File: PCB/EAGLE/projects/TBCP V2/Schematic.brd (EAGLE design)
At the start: 160 x 71.1 mm, 111 parts, among them J1 FP Header, J100 ADS1115, J2 12 Supply, J3 TB Header, Q1 DMP4025LK3Q-13, U1 ESP32-DEVKITC, U100 TLE9201SG, U2 7805

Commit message: TBCP 2.0 for review
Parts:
- removed SJ1: SOLDERJUMPERTRACE, SparkFun-Retired:SJ_2S-TRACE
- removed SW1: (no value), One_Dimensional_Pong:SWITCH_SPST_SMD_A
- added S5: 500SSP1S1M6QEA, 500SSP1S1M6QEA:500SSP1S1M6QEA
- R1, R11, R2, R3, R5, R8: value (none) -> 150
- R10, R4, R7: value 8000 -> 5k
- R13, R14, R15, R16: value (none) -> 5k
- S1, S2, S3, S4: value (none) -> MOMENTARY-SWITCH-SPST-PTH-6.0MM-KIT; device SparkFun-Retired:TACTILE-SWITCH-SMD -> SparkFun-Switches:TACTILE_SWITCH_PTH_6.0MM_KIT
- moved Q1 6.48 mm to (102.9, 7.62)
- moved Z1 6.48 mm to (111.8, 7.62)
- moved R17 6.48 mm to (115.6, 7.62)
- moved J2 4.58 mm to (62.2, 10.2)
- moved S1 2.84 mm to (19.1, 7.62)
- moved S2 2.84 mm to (29.2, 7.62)
- moved S3 2.84 mm to (39.4, 7.62)
- moved S4 2.84 mm to (49.5, 7.62)
- moved TP104 2.62 mm to (80.0, 43.2)
- moved TP105 1.42 mm to (80.0, 45.7)
- moved TP101 1.27 mm to (80.0, 40.6)
- moved TP102 1.27 mm to (80.0, 35.6)
- moved TP106 0.63 mm to (80.0, 48.3)
- renumbered J100 to U4, U100 to U5
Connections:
- net 0VDC: no longer SJ1.2
- net 3.3VDC: no longer S1.4, S2.4, S3.4, S4.4
- net ADS1115_A4: no longer SJ1.1
- net GPIO34: no longer S3.2
- net GPIO35: no longer S4.2
- net GPIO36: no longer S1.2
- net GPIO39: no longer S2.2
- net N$1: now also S5.2; no longer SW1.3
- net N$36: now also S5.1; no longer SW1.2
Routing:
- net GPIO27: track 80.9 -> 48.5 mm
- net N$1: track 0.00 -> 26.6 mm
- net GPIO35: track 33.6 -> 21.7 mm
- net GPIO36: track 50.3 -> 38.3 mm
- net GPIO34: track 30.7 -> 18.9 mm
- net GPIO39: track 33.9 -> 22.0 mm
- net M0+: track 126.7 -> 136.5 mm
- net M0-: track 133.1 -> 140.3 mm
- net N$36: track 10.5 -> 15.9 mm
- net 12VDC: track 126.2 -> 130.8 mm
- net ADS1115_A4: track 6.48 -> 3.81 mm
- net GPIO26: track 73.2 -> 71.4 mm
- added copper zone on layer 16, net 0VDC
- removed copper zone on layer 16, net 0VDC1
- removed copper zone on layer 1, net N$1
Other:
- board text added: "Project: Throttle Body Control Platform By: Oliver Bell, Piyapat Srisawat Date: 01/08/2024 Version: 2.0"
- board text removed: "Project: Throttle body control Platform By: Oliver Bell, Piyapat Srisawat Date: 01/08/2024 Version: 2.0"

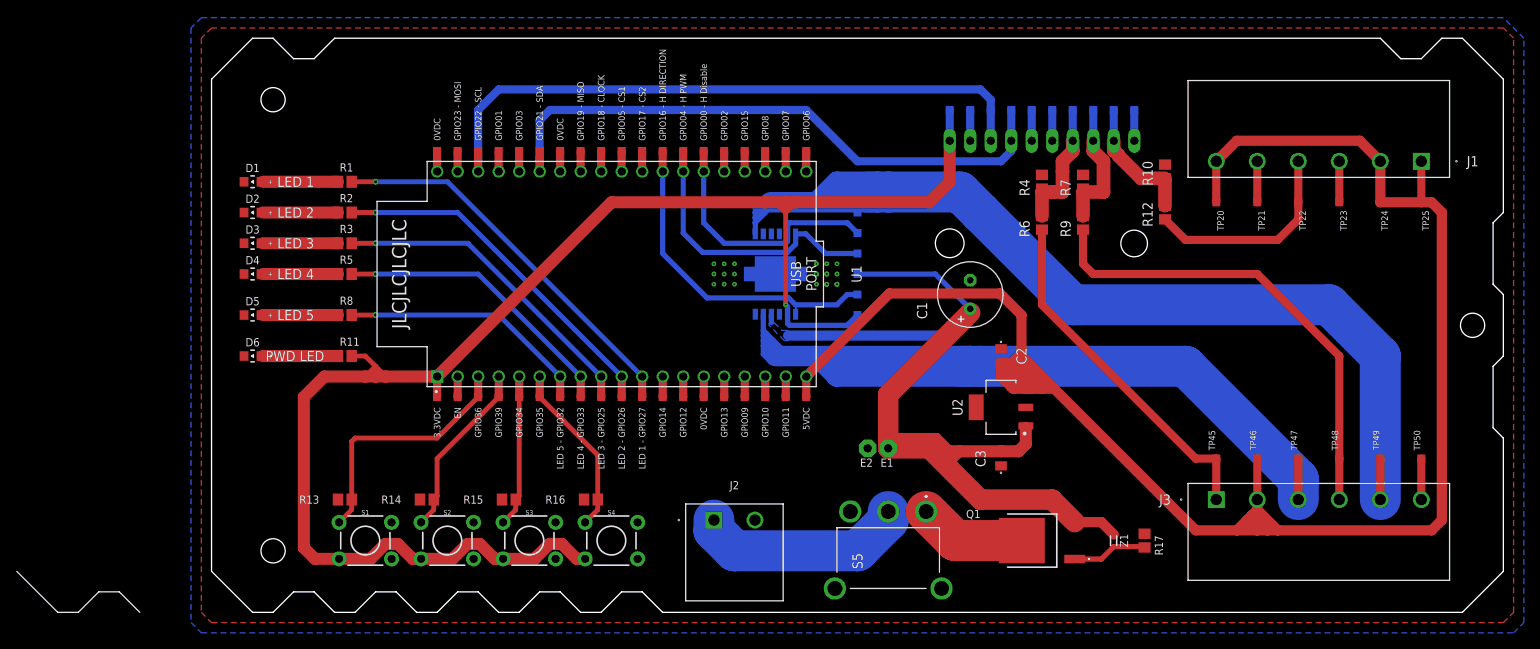
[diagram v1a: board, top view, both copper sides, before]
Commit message: Major rename of folder
matlab doesnt like have spaces in names of files or folders
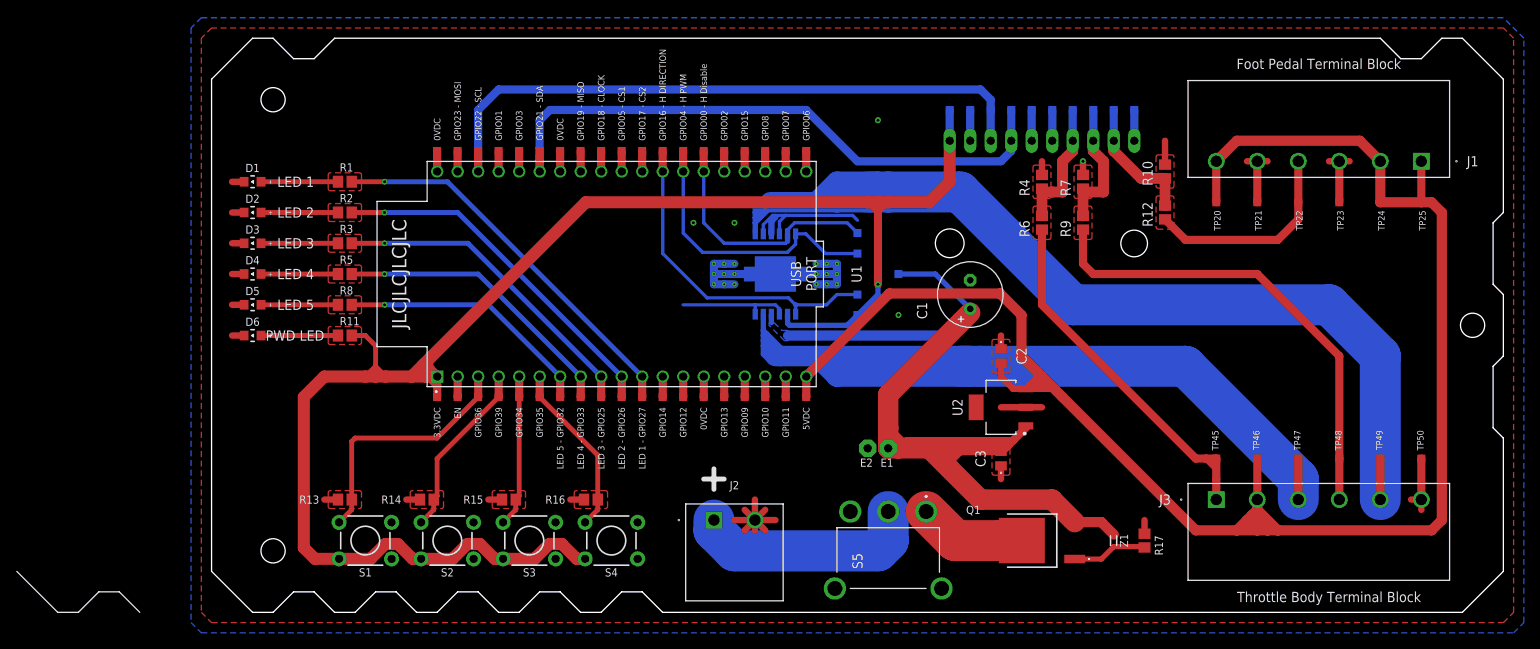
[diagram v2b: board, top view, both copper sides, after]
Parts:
- moved TP101 5.08 mm to (85.1, 40.6)
- moved D6 2.54 mm to (5.08, 33.0)
- moved R11 2.54 mm to (16.5, 33.0)
- moved TP106 1.27 mm to (80.0, 49.5)
- moved D5 1.27 mm to (5.08, 36.8)
- moved R8 1.27 mm to (16.5, 36.8)
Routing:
- net 0VDC: track 26.7 -> 144.6 mm, vias 22 -> 23
- net 12VDC: track 130.8 -> 147.8 mm
- net 3.3VDC: track 198.8 -> 211.4 mm
- net 5VDC: track 231.2 -> 222.1 mm
- net TB_FB_INV: track 43.9 -> 46.9 mm
- net N$1: track 26.6 -> 28.0 mm
- net M0-: track 140.3 -> 139.1 mm
- net N$2: track 9.53 -> 10.2 mm
- net GPIO32: track 31.5 -> 32.1 mm
- added copper zone on layer 1, net 0VDC17
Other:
- board text added: "0VDC 6."
- board text added: "1. 5VDC"
- board text added: "5VDC 2."
- board text added: "Foot Pedal Terminal Block"
- board text added: "M0+ 3."
- board text added: "M0- 5."
- board text added: "TB_FB 4."
- board text added: "TB_FB_INV 1."
- board text added: "Throttle Body Terminal Block"

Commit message: TBCP 2.0 sent to JLCPCB
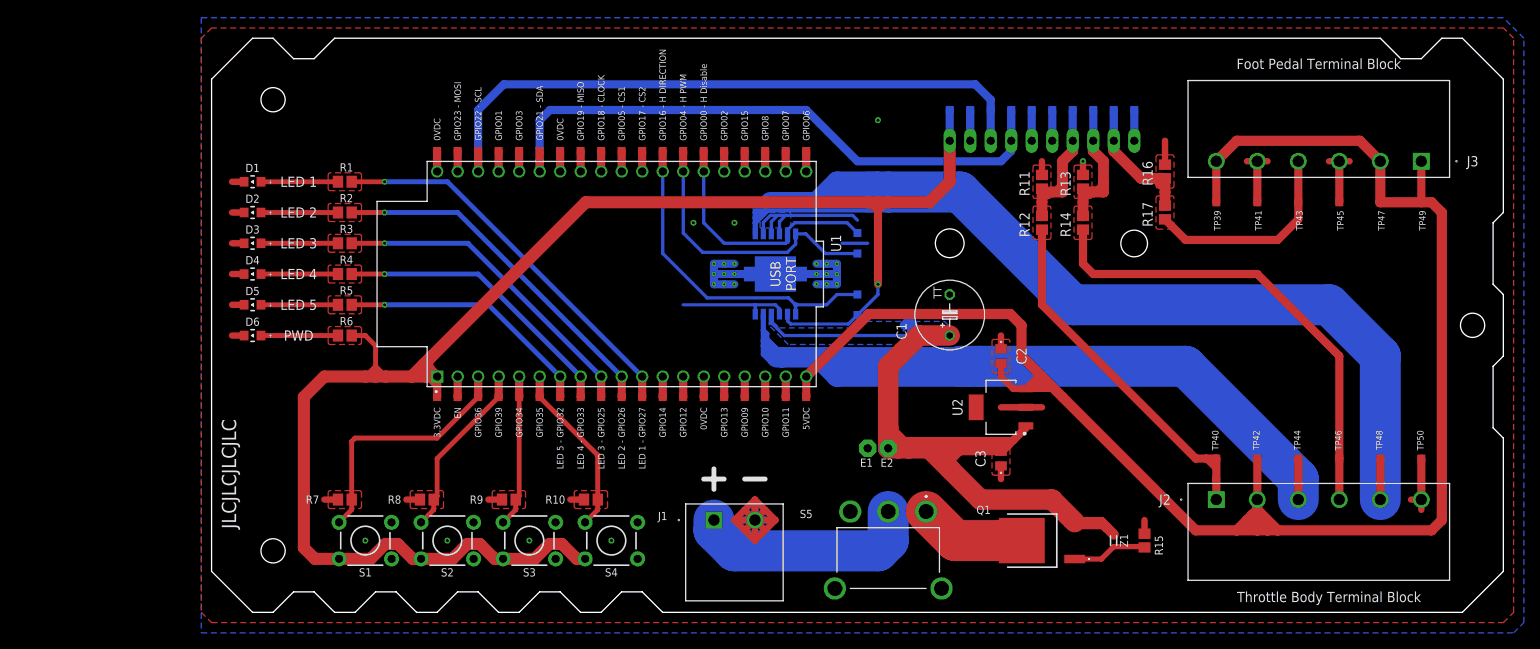
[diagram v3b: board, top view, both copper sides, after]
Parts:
- C1: device BeagleBone_Blue_R3:E3,5-8 -> BeagleBone_Blue_R3:TAP5-80
- J1: value FP Header -> 12 Supply; device Terminal 5.08 Pitch 6S 1757284:1757284 -> Terminal 5.08 Pitch 2S :1757284
- J2: value 12 Supply -> TB Header; device Terminal 5.08 Pitch 2S :1757284 -> Terminal 5.08 Pitch 6S 1757284:1757284
- J3: value TB Header -> FP Header
- R11, R8: value 150 -> 5k
- R14: value 5k -> 100k
- R15: value 5k -> 100K
- R17: value 100K -> 100k
- R4: value 5k -> 150
- R6: value 100k -> 150
- R9: value 100k -> 5k
- TP10: value TESTPOINT_TPS-SMD-10SN -> GPIO34
- TP12: value TESTPOINT_TPS-SMD-10SN -> GPIO35
- TP14: value TESTPOINT_TPS-SMD-10SN -> GPIO32
- TP2: value TESTPOINT_TPS-SMD-10SN -> 3V3
- TP26: value 3V3 -> TESTPOINT_TPS-SMD-10SN
- TP27: value EN -> TESTPOINT_TPS-SMD-10SN
- TP28: value GPIO36 -> TESTPOINT_TPS-SMD-10SN
- TP29: value GPIO39 -> TESTPOINT_TPS-SMD-10SN
- TP30: value GPIO34 -> TESTPOINT_TPS-SMD-10SN
- TP31: value GPIO35 -> TESTPOINT_TPS-SMD-10SN
- TP32: value GPIO32 -> TESTPOINT_TPS-SMD-10SN
- TP4: value TESTPOINT_TPS-SMD-10SN -> EN
- TP6: value TESTPOINT_TPS-SMD-10SN -> GPIO36
- TP8: value TESTPOINT_TPS-SMD-10SN -> GPIO39
- moved R13 99.6 mm to (108.0, 52.1), turned to 270 degrees
- moved R7 99.6 mm to (16.5, 12.7), turned to 180 degrees
- moved J1 98.3 mm to (62.2, 10.2), turned to 0 degrees
- moved TP24 92.1 mm to (55.9, 25.4)
- moved TP25 91.7 mm to (58.4, 55.9), turned to 90 degrees
- moved R11 88.4 mm to (102.9, 52.1), turned to 270 degrees
- moved R14 88.2 mm to (108.0, 47.0), turned to 270 degrees
- moved R6 87.5 mm to (16.5, 33.0), turned to 0 degrees
- moved R4 87.1 mm to (16.5, 40.6), turned to 0 degrees
- moved TP22 84.8 mm to (53.3, 25.4)
- moved TP23 84.1 mm to (55.9, 55.9), turned to 90 degrees
- moved R10 81.9 mm to (47.0, 12.7), turned to 180 degrees
- moved R16 81.9 mm to (118.1, 53.3), turned to 270 degrees
- moved R9 79.0 mm to (36.8, 12.7), turned to 180 degrees
- moved R15 78.9 mm to (115.6, 7.62), turned to 270 degrees
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- renumbered U4 to U100, U5 to U101
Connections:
- net 0VDC: now also E1.PAD, J1.2, J2.6, J3.3, J3.5, R10.2, R11.1, R13.1, R15.1, R16.1, R7.2, R8.2, R9.2, TP108.TP, TP13.TP, TP28.TP, TP41.TP, TP45.TP; no longer E2.PAD, J1.3, J1.5, J2.2, J3.6, R10.1, R13.2, R14.2, R15.2, R16.2, R17.1, R4.1, R7.1, TP115.TP, TP21.TP, TP23.TP, TP39.TP, TP7.TP
- net 12VDC: now also E2.PAD, TP110.TP; no longer E1.PAD, TP101.TP
- net 3.3VDC: now also R6.2, TP109.TP, TP112.TP, TP2.TP; no longer R11.2, TP102.TP, TP116.TP, TP26.TP
- net 5VDC: now also J2.2, J3.1, J3.6, TP38.TP, TP39.TP, TP42.TP, TP47.TP, TP49.TP; no longer J1.1, J1.2, J1.6, TP20.TP, TP24.TP, TP25.TP, TP44.TP, TP46.TP
- net ADDR: now also TP105.TP; no longer TP112.TP
- net ADS1115_A0: now also R11.2, R12.1, TP103.TP; no longer R4.2, R6.1, TP110.TP
- net ADS1115_A1: now also R13.2, R14.1, TP102.TP; no longer R7.2, R9.1, TP109.TP
- net ADS1115_A2: now also R16.2, R17.1, TP101.TP; no longer R10.2, R12.1, TP108.TP
- net ADS1115_A4: now also TP100.TP; no longer TP107.TP
- net EN: now also TP4.TP; no longer TP27.TP
- net FP_FB: now also J3.4, R17.2, TP43.TP; no longer J1.4, R12.2, TP22.TP
- net GPIO01: now also TP7.TP; no longer TP4.TP
- net GPIO02: now also TP29.TP; no longer TP15.TP
- net GPIO03: now also TP9.TP; no longer TP5.TP
- net GPIO06: now also TP37.TP; no longer TP19.TP
- net GPIO07: now also TP35.TP; no longer TP18.TP
- net GPIO08: now also TP33.TP; no longer TP17.TP
- net GPIO09: now also TP32.TP; no longer TP41.TP
- net GPIO10: now also TP34.TP; no longer TP42.TP
- net GPIO11: now also TP36.TP; no longer TP43.TP
- net GPIO12: now also TP26.TP; no longer TP38.TP
- net GPIO13: now also TP30.TP; no longer TP40.TP
- net GPIO14: now also TP24.TP; no longer TP37.TP
- net GPIO15: now also TP31.TP; no longer TP16.TP
- net GPIO25: now also TP18.TP; no longer TP34.TP
- net GPIO26: now also TP20.TP; no longer TP35.TP
- net GPIO27: now also TP22.TP; no longer TP36.TP
- net GPIO32: now also R5.2, TP14.TP; no longer R8.2, TP32.TP
- net GPIO33: now also R4.2, TP16.TP; no longer R5.2, TP33.TP
- net GPIO34: now also R9.1, TP10.TP; no longer R15.1, TP30.TP
- net GPIO35: now also R10.1, TP12.TP; no longer R16.1, TP31.TP
- net GPIO36: now also R7.1, TP6.TP; no longer R13.1, TP28.TP
- net GPIO39: now also R8.1, TP8.TP; no longer R14.1, TP29.TP
- net HBRDIGE_DISABLE: now also TP115.TP, TP27.TP; no longer TP105.TP, TP14.TP
- net HBRIDGE_DIRECTION: now also TP113.TP, TP23.TP; no longer TP103.TP, TP12.TP
- net HBRIDGE_PWM: now also TP114.TP, TP25.TP; no longer TP104.TP, TP13.TP
- net M0+: now also J2.3, TP111.TP, TP44.TP; no longer J3.3, TP100.TP, TP47.TP
- net M0-: now also J2.5, TP116.TP, TP48.TP; no longer J3.5, TP106.TP, TP49.TP
- net N$1: now also J1.1; no longer J2.1
- net N$12: now also R4.1; no longer R5.1
- net N$13: now also R5.1; no longer R8.1
- net N$2: now also R6.1; no longer R11.1
- net N$41: now also TP104.TP; no longer TP111.TP
- net N$7: now also R15.2; no longer R17.2
- net SCL: now also TP107.TP, TP5.TP; no longer TP114.TP, TP3.TP
- net SDA: now also TP106.TP, TP11.TP; no longer TP113.TP, TP6.TP
- net SPI_CLOCK: now also TP17.TP; no longer TP9.TP
- net SPI_CS1: now also TP19.TP; no longer TP10.TP
- net SPI_CS2: now also TP21.TP; no longer TP11.TP
- net SPI_MISO: now also TP15.TP; no longer TP8.TP
- net SPI_MOSI: now also TP3.TP; no longer TP2.TP
- net TB_FB: now also J2.4, R14.2, TP46.TP; no longer J3.4, R9.2, TP48.TP
- net TB_FB_INV: now also J2.1, R12.2, TP40.TP; no longer J3.1, R6.2, TP45.TP
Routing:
- net 0VDC: track 144.6 -> 167.7 mm, vias 23 -> 26
- net ADS1115_A1: track 16.6 -> 21.3 mm
- net ADS1115_A0: track 16.6 -> 20.2 mm
- net 5VDC: track 222.1 -> 219.3 mm
- net M0+: track 136.5 -> 133.9 mm
- net ADS1115_A2: track 16.2 -> 18.4 mm
- net SCL: track 80.3 -> 80.9 mm
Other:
- board text added: "12V"
- board text added: "2. 5VDC"
- board text added: "3. 0VDC"
- board text added: "4. FP_FB"
- board text added: "5. 0VDC"
- board text added: "6. 5VDC"
- board text added: "Heat Sink Alignment"
- board text added: "O.B"
- board text added: "PWD"
- board text removed: "PWD LED"
